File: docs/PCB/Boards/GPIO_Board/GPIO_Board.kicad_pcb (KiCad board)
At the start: 2 copper layers, 64.2 x 35.6 mm, 25 parts, among them J1 COM, J2 GPIO, Q1 AO3407A, SW1 SW_DIP_x03, SW2 Tact Switch 6x6mm / 13mm, U1 MCP23017_SS, U2 SIP32431DR3-T1GE3

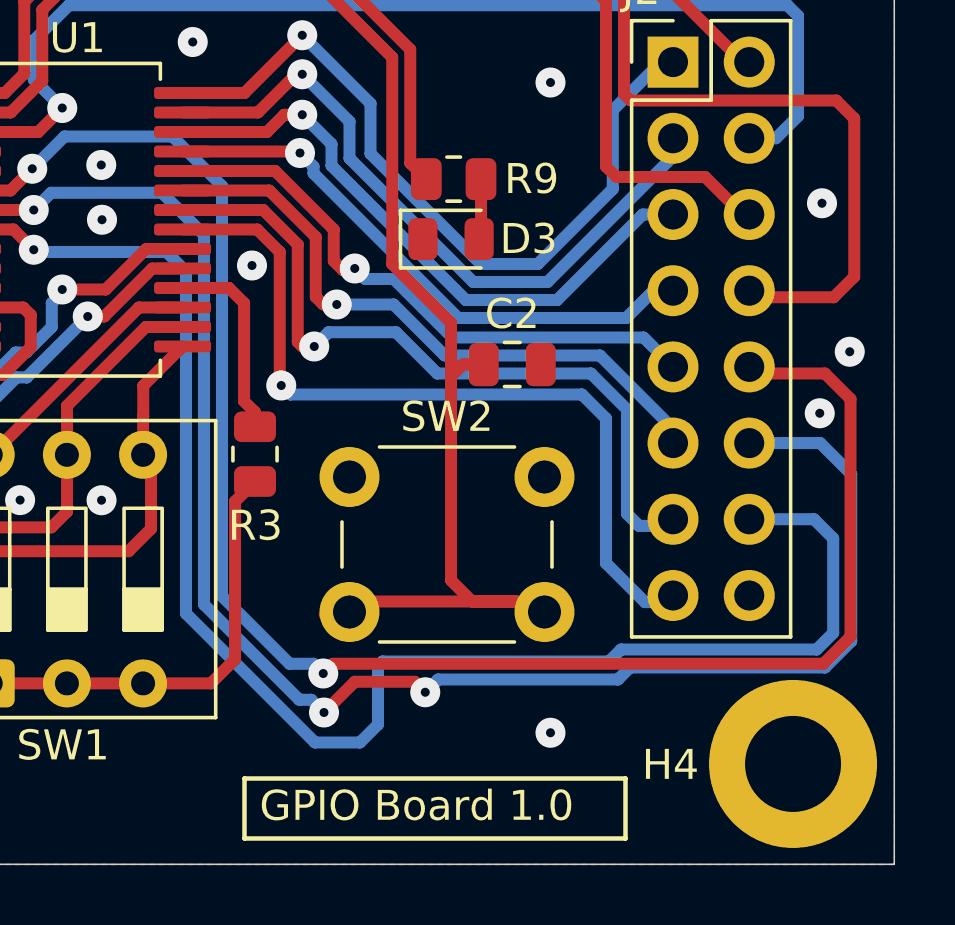
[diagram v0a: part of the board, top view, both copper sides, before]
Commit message: Test program added, can protocol added.
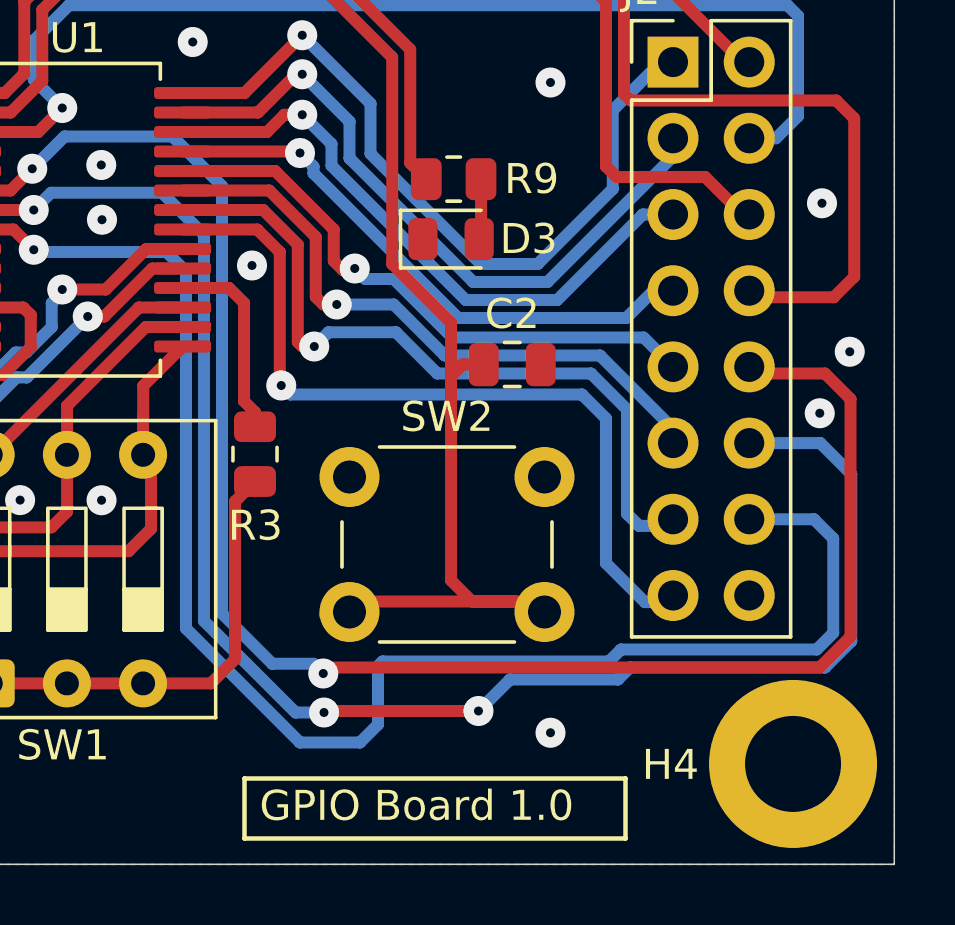
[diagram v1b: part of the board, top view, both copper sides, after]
